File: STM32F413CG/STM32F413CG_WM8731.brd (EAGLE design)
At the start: 54 x 33 mm, 59 parts, among them IC1 STM32F413CGU6, IC2 WM8731SEDS_RV, J2 1503_02, X1 USB-MICROB-SMD

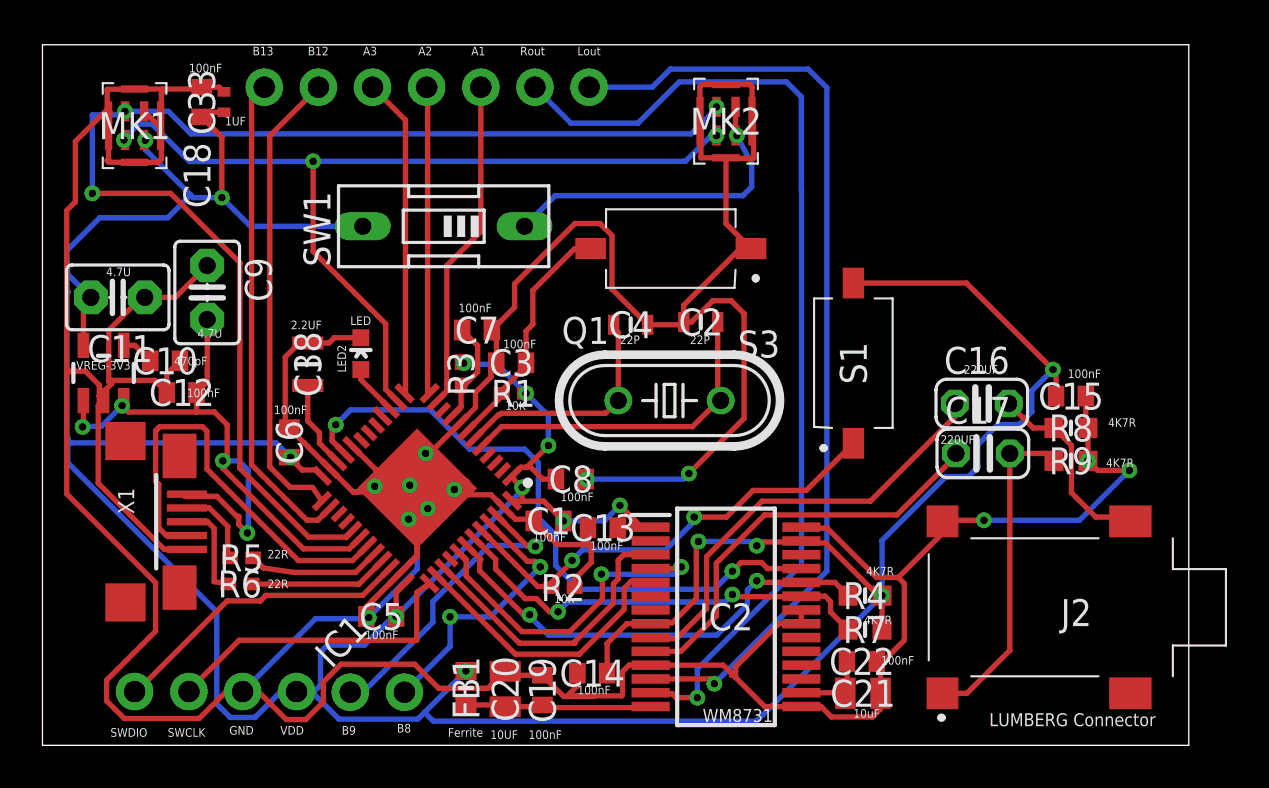
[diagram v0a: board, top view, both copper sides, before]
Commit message: added STM32L451RE
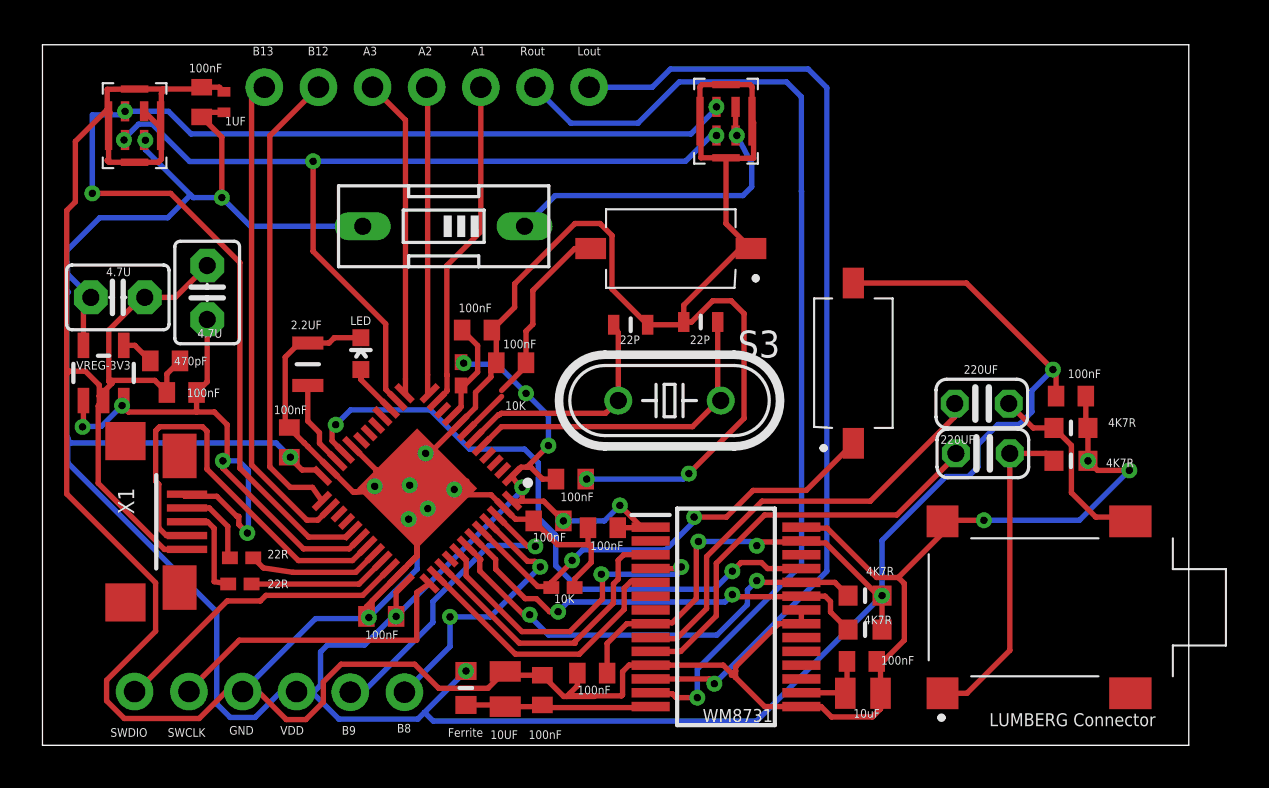
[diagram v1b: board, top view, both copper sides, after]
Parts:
- removed R1: CRCW040210K0JNED, CRCW040210K0JNED:RESC1005X40N
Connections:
- net N$3: no longer R1.2
- net VDD: no longer R1.1
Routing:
- net A1: track 16.2 -> 15.7 mm
